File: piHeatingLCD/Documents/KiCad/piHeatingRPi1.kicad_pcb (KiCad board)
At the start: 2 copper layers, 64.8 x 50.8 mm, 17 parts, among them J1 Raspberry_Pi_1_all_pin_ordered, J2 10-pin_header_LCD_interface, J3 3-pin_KY-019_relay_header, J4 3_pin_Dallas_1-wire_connector, J5 2-pin_NO_switch_header, J6 2-pin_NO_switch_header, J7 2-pin_NO_switch_header, J8 2-pin_NO_switch_header

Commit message: updated kicad
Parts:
- added D1: LED, My_Misc:CP_Radial_D5.0mm_P2.50mm_larger_pads, F.Cu at (151.8, 66.0)
- added R10: R, My_Misc:R_Axial_DIN0207_L6.3mm_D2.5mm_P10.16mm_Horizontal_larger_pads, F.Cu at (150.5, 56.5)
- moved J3 28.7 mm to (151.8, 73.7)
- moved J4 12.5 mm to (160.0, 59.7)
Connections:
- J1 pad 10: Net-(J1-Pad10) -> Net-(D1-Pad2)
- J3 pad 1: Net-(J1-Pad8) -> Net-(D1-Pad2)
- J3 pad 2: Net-(J1-Pad1) -> Net-(J1-Pad2)
- J4 pad 2: Net-(J1-Pad10) -> Net-(J1-Pad8)
- R1 pad 1: Net-(J1-Pad1) -> Net-(J1-Pad2)
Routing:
- net Net-(D1-Pad2): track 0.00 -> 82.8 mm
- net Net-(J1-Pad10): track 57.4 -> 0.00 mm
- net Net-(J1-Pad2): track 47.7 -> 71.9 mm
- net Net-(J1-Pad1): track 78.4 -> 58.5 mm, vias 4 -> 2
- net Net-(J1-Pad8): track 40.4 -> 52.7 mm
- net Net-(D1-Pad1): track 0.00 -> 10.1 mm
- net Net-(J1-Pad25): track 98.9 -> 99.8 mm, vias 0 -> 2
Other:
- board size 64.8 x 50.8 mm -> 64.1 x 49.5 mm
- board text added: "GND"

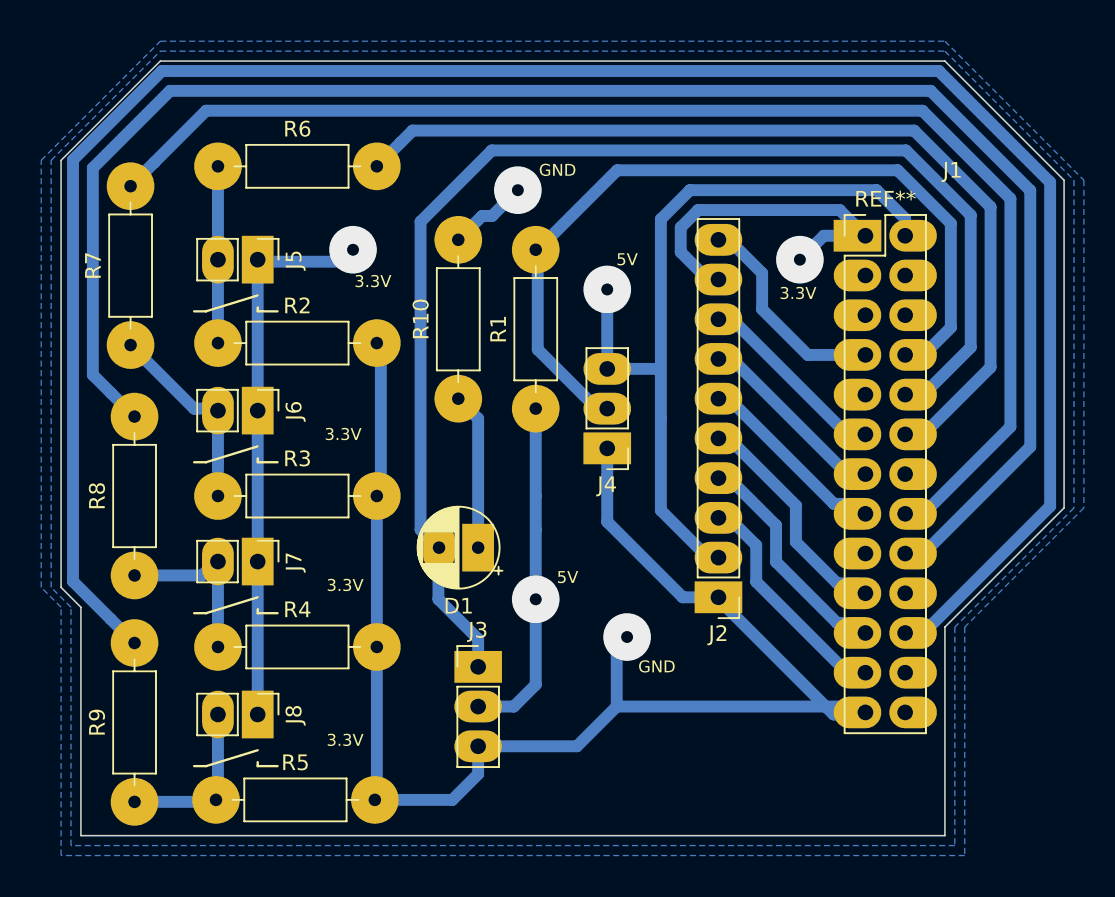
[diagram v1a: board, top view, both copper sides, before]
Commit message: moved dallas from 5V to 3.3V
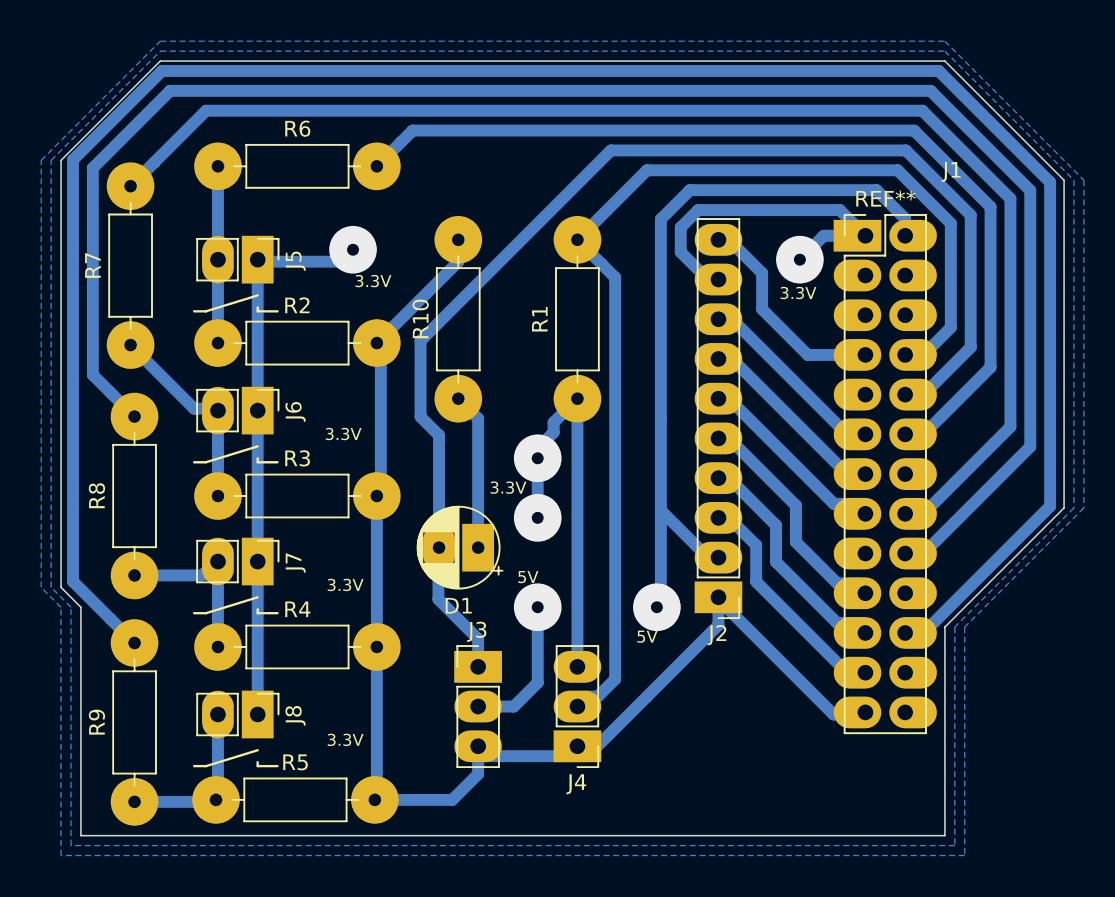
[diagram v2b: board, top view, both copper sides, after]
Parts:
- R10: value R -> 120R
- moved J4 19.1 mm to (158.1, 78.7)
- moved R1 2.74 mm to (158.1, 56.5)
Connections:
- net Net-(J1-Pad25) renamed /GND
- J1 pad 1: Net-(J1-Pad1) -> /3.3V
- J1 pad 2: Net-(J1-Pad2) -> /5V
- J2 pad 2: Net-(J1-Pad2) -> /5V
- J2 pad 9: Net-(J1-Pad1) -> /3.3V
- J3 pad 2: Net-(J1-Pad2) -> /5V
- J4 pad 3: Net-(J1-Pad2) -> /3.3V
- J5 pad 1: Net-(J1-Pad1) -> /3.3V
- J6 pad 1: Net-(J1-Pad1) -> /3.3V
- J7 pad 1: Net-(J1-Pad1) -> /3.3V
- J8 pad 1: Net-(J1-Pad1) -> /3.3V
- R1 pad 1: Net-(J1-Pad2) -> /3.3V
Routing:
- net /3.3V: track 0.00 -> 84.3 mm, vias 0 -> 4
- net Net-(J1-Pad2): track 71.9 -> 0.00 mm, vias 2 -> 0
- net Net-(J1-Pad1): track 58.5 -> 0.00 mm, vias 2 -> 0
- net /5V: track 0.00 -> 57.6 mm, vias 0 -> 2
- net /GND: track 99.8 -> 79.7 mm, vias 2 -> 0
- net Net-(J1-Pad8): track 52.7 -> 69.8 mm
- net Net-(D1-Pad2): track 82.8 -> 78.1 mm
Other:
- board text removed: "GND"
